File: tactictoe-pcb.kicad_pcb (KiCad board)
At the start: 4 copper layers, 85.6 x 54 mm, 90 parts, among them J1 USB_C_Receptacle_USB2.0_16P, J2 Conn_01x04, T1 Touchpad, T2 Touchpad, T3 Touchpad, T4 Touchpad, T5 Touchpad, T6 Touchpad, T7 Touchpad, T8 Touchpad, T9 Touchpad, U2 TLV74033PDBVR

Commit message: major v2 changes
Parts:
- removed R1, R2, R3: 10k, Resistor_SMD:R_0603_1608Metric_Pad0.98x0.95mm_HandSolder
- removed TP1: NRST, TestPoint:TestPoint_Pad_D1.0mm
- removed TP2: PF0, TestPoint:TestPoint_Pad_D1.0mm
- removed TP3: PF1, TestPoint:TestPoint_Pad_D1.0mm
- removed TP4: PB8, TestPoint:TestPoint_Pad_D1.0mm
- removed TP5: PA15, TestPoint:TestPoint_Pad_D1.0mm
- C1, C2, C3, C4, C5, C6, C7, C8, C9: footprint Capacitor_SMD:C_0603_1608Metric_Pad1.08x0.95mm_HandSolder -> Capacitor_SMD:C_0603_1608Metric
- D1, D10, D11, D12, D13, D14, D15, D16, D17, D18, D19, D2, D20, D21, D22, D23, D24, D25, D26, D27, D28, D29, D3, D30, D31, D32, D33, D34, D35, D36, D37, D38, D39, D4, D40, D41, D42, D43, D44, D45, D5, D6, D7, D8, D9: value SK6805-EC15 -> XL-1615RGBC; footprint tictactoe-bolt-footprints:SK6805-EC15 -> tactictoe-footprints:XL-1615RGBC-WS2812B-S
- J1: footprint tictactoe-bolt-footprints:USB_C_Receptacle_TYPE-C-16P-CB1-6-073 -> tactictoe-footprints:USB_C_Receptacle_TYPE-C-16P-CB1-6-073
- J2: footprint Connector_PinHeader_2.54mm:PinHeader_1x04_P2.54mm_Vertical -> tactictoe-footprints:tactictoe-sw-pins; moved to B.Cu
- R10, R11, R12, R13, R14, R4, R5, R6, R7, R8, R9: footprint Resistor_SMD:R_0603_1608Metric_Pad0.98x0.95mm_HandSolder -> Resistor_SMD:R_0603_1608Metric
- T1, T2, T3, T4, T5, T6, T7, T8, T9: footprint tictactoe-bolt-footprints:Touch-pad -> tactictoe-footprints:Touch-pad_XL-1615
- U1: value ~ -> F042G6U6TR
- moved R6 21.5 mm to (117.0, 103.1), turned to -90 degrees
- moved R7 19.4 mm to (118.5, 103.1), turned to -90 degrees
- moved R8 17.3 mm to (120.0, 103.1), turned to -90 degrees
- moved C6 15.1 mm to (115.2, 110.8)
- moved C7 15.1 mm to (113.7, 110.8)
- moved C5 14.0 mm to (123.0, 112.0)
- moved C9 14.0 mm to (124.5, 112.0)
- moved U1 14.0 mm to (119.0, 111.0)
- moved C3 13.4 mm to (117.0, 116.9)
- moved C4 13.4 mm to (115.5, 116.9)
- moved C1 11.5 mm to (108.3, 107.0), turned to -90 degrees
- moved R14 11.1 mm to (119.9, 116.9), turned to 90 degrees
- moved C8 10.8 mm to (123.0, 103.1), turned to 90 degrees
- moved R13 9.15 mm to (121.4, 116.9), turned to 90 degrees
- moved R12 7.28 mm to (122.9, 116.9), turned to 90 degrees
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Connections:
- D1 pad 1: /LED_CH4 -> GND
- D1 pad 2: +5V -> /LED_T3C4
- D1 pad 3: Net-(D1-DOUT) -> +5V
- D1 pad 4: GND -> Net-(D1-DOUT)
- D10 pad 1: Net-(D10-DIN) -> GND
- D10 pad 2: +5V -> Net-(D10-DIN)
- D10 pad 3: Net-(D10-DOUT) -> +5V
- D10 pad 4: GND -> Net-(D10-DOUT)
- D11 pad 1: Net-(D10-DOUT) -> GND
- D11 pad 2: +5V -> Net-(D10-DOUT)
- D11 pad 3: Net-(D11-DOUT) -> +5V
- D11 pad 4: GND -> Net-(D11-DOUT)
- D12 pad 1: Net-(D11-DOUT) -> GND
- D12 pad 2: +5V -> Net-(D11-DOUT)
- D12 pad 3: Net-(D12-DOUT) -> +5V
- D12 pad 4: GND -> Net-(D12-DOUT)
- D13 pad 1: Net-(D12-DOUT) -> GND
- D13 pad 2: +5V -> Net-(D12-DOUT)
- D13 pad 3: Net-(D13-DOUT) -> +5V
- D13 pad 4: GND -> Net-(D13-DOUT)
- D14 pad 1: Net-(D13-DOUT) -> GND
- D14 pad 2: +5V -> Net-(D13-DOUT)
- D14 pad 3: Net-(D14-DOUT) -> +5V
- D14 pad 4: GND -> Net-(D14-DOUT)
- D15 pad 1: Net-(D14-DOUT) -> GND
- D15 pad 2: +5V -> Net-(D14-DOUT)
- D15 pad 3: unconnected-(D15-DOUT-Pad3) -> +5V
- D15 pad 4: GND -> unconnected-(D15-DOUT-Pad4)
- D16 pad 1: /LED_CH3 -> GND
- D16 pad 2: +5V -> /LED_T3C3
- D16 pad 3: Net-(D16-DOUT) -> +5V
- D16 pad 4: GND -> Net-(D16-DOUT)
- D17 pad 1: Net-(D16-DOUT) -> GND
- D17 pad 2: +5V -> Net-(D16-DOUT)
- D17 pad 3: Net-(D17-DOUT) -> +5V
- D17 pad 4: GND -> Net-(D17-DOUT)
- D18 pad 1: Net-(D17-DOUT) -> GND
- D18 pad 2: +5V -> Net-(D17-DOUT)
- D18 pad 3: Net-(D18-DOUT) -> +5V
- D18 pad 4: GND -> Net-(D18-DOUT)
- D19 pad 1: Net-(D18-DOUT) -> GND
- D19 pad 2: +5V -> Net-(D18-DOUT)
- D19 pad 3: Net-(D19-DOUT) -> +5V
- D19 pad 4: GND -> Net-(D19-DOUT)
- D2 pad 1: Net-(D1-DOUT) -> GND
- D2 pad 2: +5V -> Net-(D1-DOUT)
- D2 pad 3: Net-(D2-DOUT) -> +5V
- D2 pad 4: GND -> Net-(D2-DOUT)
- D20 pad 1: Net-(D19-DOUT) -> GND
- D20 pad 2: +5V -> Net-(D19-DOUT)
- D20 pad 3: Net-(D20-DOUT) -> +5V
- D20 pad 4: GND -> Net-(D20-DOUT)
- D21 pad 1: Net-(D20-DOUT) -> GND
- D21 pad 2: +5V -> Net-(D20-DOUT)
- D21 pad 3: Net-(D21-DOUT) -> +5V
- D21 pad 4: GND -> Net-(D21-DOUT)
- D22 pad 1: Net-(D21-DOUT) -> GND
- D22 pad 2: +5V -> Net-(D21-DOUT)
- D22 pad 3: Net-(D22-DOUT) -> +5V
- D22 pad 4: GND -> Net-(D22-DOUT)
- D23 pad 1: Net-(D22-DOUT) -> GND
- D23 pad 2: +5V -> Net-(D22-DOUT)
- D23 pad 3: Net-(D23-DOUT) -> +5V
- D23 pad 4: GND -> Net-(D23-DOUT)
- D24 pad 1: Net-(D23-DOUT) -> GND
- D24 pad 2: +5V -> Net-(D23-DOUT)
- D24 pad 3: Net-(D24-DOUT) -> +5V
- D24 pad 4: GND -> Net-(D24-DOUT)
- D25 pad 1: Net-(D24-DOUT) -> GND
- D25 pad 2: +5V -> Net-(D24-DOUT)
- D25 pad 3: Net-(D25-DOUT) -> +5V
- D25 pad 4: GND -> Net-(D25-DOUT)
- D26 pad 1: Net-(D25-DOUT) -> GND
- D26 pad 2: +5V -> Net-(D25-DOUT)
- D26 pad 3: Net-(D26-DOUT) -> +5V
- D26 pad 4: GND -> Net-(D26-DOUT)
- D27 pad 1: Net-(D26-DOUT) -> GND
- D27 pad 2: +5V -> Net-(D26-DOUT)
- D27 pad 3: Net-(D27-DOUT) -> +5V
- D27 pad 4: GND -> Net-(D27-DOUT)
- D28 pad 1: Net-(D27-DOUT) -> GND
- D28 pad 2: +5V -> Net-(D27-DOUT)
- D28 pad 3: Net-(D28-DOUT) -> +5V
- D28 pad 4: GND -> Net-(D28-DOUT)
- D29 pad 1: Net-(D28-DOUT) -> GND
- D29 pad 2: +5V -> Net-(D28-DOUT)
- D29 pad 3: Net-(D29-DOUT) -> +5V
- D29 pad 4: GND -> Net-(D29-DOUT)
- D3 pad 1: Net-(D2-DOUT) -> GND
- D3 pad 2: +5V -> Net-(D2-DOUT)
- D3 pad 3: Net-(D3-DOUT) -> +5V
- D3 pad 4: GND -> Net-(D3-DOUT)
- D30 pad 1: Net-(D29-DOUT) -> GND
- D30 pad 2: +5V -> Net-(D29-DOUT)
- D30 pad 3: unconnected-(D30-DOUT-Pad3) -> +5V
- D30 pad 4: GND -> unconnected-(D30-DOUT-Pad4)
- D31 pad 1: /LED_CH2 -> GND
- D31 pad 2: +5V -> /LED_T16C1
- D31 pad 3: Net-(D31-DOUT) -> +5V
- D31 pad 4: GND -> Net-(D31-DOUT)
- D32 pad 1: Net-(D31-DOUT) -> GND
- D32 pad 2: +5V -> Net-(D31-DOUT)
- D32 pad 3: Net-(D32-DOUT) -> +5V
- D32 pad 4: GND -> Net-(D32-DOUT)
- D33 pad 1: Net-(D32-DOUT) -> GND
- D33 pad 2: +5V -> Net-(D32-DOUT)
- D33 pad 3: Net-(D33-DOUT) -> +5V
- D33 pad 4: GND -> Net-(D33-DOUT)
- D34 pad 1: Net-(D33-DOUT) -> GND
- D34 pad 2: +5V -> Net-(D33-DOUT)
- D34 pad 3: Net-(D34-DOUT) -> +5V
- D34 pad 4: GND -> Net-(D34-DOUT)
- D35 pad 1: Net-(D34-DOUT) -> GND
- D35 pad 2: +5V -> Net-(D34-DOUT)
- D35 pad 3: Net-(D35-DOUT) -> +5V
- D35 pad 4: GND -> Net-(D35-DOUT)
- D36 pad 1: Net-(D35-DOUT) -> GND
- D36 pad 2: +5V -> Net-(D35-DOUT)
- D36 pad 3: Net-(D36-DOUT) -> +5V
- D36 pad 4: GND -> Net-(D36-DOUT)
- D37 pad 1: Net-(D36-DOUT) -> GND
- D37 pad 2: +5V -> Net-(D36-DOUT)
- D37 pad 3: Net-(D37-DOUT) -> +5V
- D37 pad 4: GND -> Net-(D37-DOUT)
- D38 pad 1: Net-(D37-DOUT) -> GND
- D38 pad 2: +5V -> Net-(D37-DOUT)
- D38 pad 3: Net-(D38-DOUT) -> +5V
- D38 pad 4: GND -> Net-(D38-DOUT)
- D39 pad 1: Net-(D38-DOUT) -> GND
- D39 pad 2: +5V -> Net-(D38-DOUT)
- D39 pad 3: Net-(D39-DOUT) -> +5V
- D39 pad 4: GND -> Net-(D39-DOUT)
- D4 pad 1: Net-(D3-DOUT) -> GND
- D4 pad 2: +5V -> Net-(D3-DOUT)
- D4 pad 3: Net-(D4-DOUT) -> +5V
- D4 pad 4: GND -> Net-(D4-DOUT)
- D40 pad 1: Net-(D39-DOUT) -> GND
- D40 pad 2: +5V -> Net-(D39-DOUT)
- D40 pad 3: Net-(D40-DOUT) -> +5V
- D40 pad 4: GND -> Net-(D40-DOUT)
- D41 pad 1: Net-(D40-DOUT) -> GND
- D41 pad 2: +5V -> Net-(D40-DOUT)
- D41 pad 3: Net-(D41-DOUT) -> +5V
- D41 pad 4: GND -> Net-(D41-DOUT)
- D42 pad 1: Net-(D41-DOUT) -> GND
- D42 pad 2: +5V -> Net-(D41-DOUT)
- D42 pad 3: Net-(D42-DOUT) -> +5V
- D42 pad 4: GND -> Net-(D42-DOUT)
- D43 pad 1: Net-(D42-DOUT) -> GND
- D43 pad 2: +5V -> Net-(D42-DOUT)
- D43 pad 3: Net-(D43-DOUT) -> +5V
- D43 pad 4: GND -> Net-(D43-DOUT)
- D44 pad 1: Net-(D43-DOUT) -> GND
- D44 pad 2: +5V -> Net-(D43-DOUT)
- D44 pad 3: Net-(D44-DOUT) -> +5V
- D44 pad 4: GND -> Net-(D44-DOUT)
- D45 pad 1: Net-(D44-DOUT) -> GND
- D45 pad 2: +5V -> Net-(D44-DOUT)
- D45 pad 3: unconnected-(D45-DOUT-Pad3) -> +5V
- D45 pad 4: GND -> unconnected-(D45-DOUT-Pad4)
- D5 pad 1: Net-(D4-DOUT) -> GND
- D5 pad 2: +5V -> Net-(D4-DOUT)
- D5 pad 3: Net-(D5-DOUT) -> +5V
- D5 pad 4: GND -> Net-(D5-DOUT)
- D6 pad 1: Net-(D5-DOUT) -> GND
- D6 pad 2: +5V -> Net-(D5-DOUT)
- D6 pad 3: Net-(D6-DOUT) -> +5V
- D6 pad 4: GND -> Net-(D6-DOUT)
- D7 pad 1: Net-(D6-DOUT) -> GND
- D7 pad 2: +5V -> Net-(D6-DOUT)
- D7 pad 3: Net-(D7-DOUT) -> +5V
- D7 pad 4: GND -> Net-(D7-DOUT)
- D8 pad 1: Net-(D7-DOUT) -> GND
- D8 pad 2: +5V -> Net-(D7-DOUT)
- D8 pad 3: Net-(D8-DOUT) -> +5V
- D8 pad 4: GND -> Net-(D8-DOUT)
- D9 pad 1: Net-(D8-DOUT) -> GND
- D9 pad 2: +5V -> Net-(D8-DOUT)
- D9 pad 3: Net-(D10-DIN) -> +5V
- D9 pad 4: GND -> Net-(D10-DIN)
- J1 pad A6: /USB_D+ -> unconnected-(J1-D+-PadA6)
- J1 pad A7: /USB_D- -> unconnected-(J1-D--PadA7)
- J1 pad B6: /USB_D+ -> unconnected-(J1-D+-PadB6)
- J1 pad B7: /USB_D- -> unconnected-(J1-D--PadB7)
- J2 pad 1: +5V -> GND
- J2 pad 4: GND -> +5V
- U1 pad 1: /PB8 -> /LED_T16C1
- U1 pad 14: /LED_CH3 -> /LED_T3C3
- U1 pad 15: /LED_CH4 -> /LED_T3C4
- U1 pad 19: /USB_D- -> unconnected-(U1-PA9/PA11-Pad19)
- U1 pad 2: /PF0 -> unconnected-(U1-PF0-Pad2)
- U1 pad 20: /USB_D+ -> unconnected-(U1-PA10/PA12-Pad20)
- U1 pad 23: /PA15 -> unconnected-(U1-PA15-Pad23)
- U1 pad 26: /LED_CH2 -> unconnected-(U1-PB5-Pad26)
- U1 pad 3: /PF1 -> unconnected-(U1-PF1-Pad3)
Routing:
- net /LED_CH4: track 34.9 -> 0.00 mm
- net /TSC_G3_IO2: track 31.0 -> 0.00 mm
- net /BTN_9: track 44.5 -> 14.9 mm
- net /LED_CH2: track 28.6 -> 0.00 mm, vias 2 -> 0
- net /TSC_G3_IO3: track 28.3 -> 0.00 mm
- net /TSC_G3_IO4: track 26.1 -> 0.00 mm
- net /LED_CH3: track 23.7 -> 0.00 mm, vias 2 -> 0
- net /SWCLK: track 20.6 -> 0.00 mm
- net /SWDIO: track 18.0 -> 0.00 mm
- net /TSC_G2_IO4: track 17.6 -> 0.00 mm
- net /TSC_G1_IO4: track 16.2 -> 0.00 mm
- net /TSC_G2_IO3: track 15.8 -> 0.00 mm
- net /TSC_G1_IO3: track 15.5 -> 0.00 mm
- net /TSC_G1_IO2: track 15.4 -> 0.00 mm
- net /TSC_G2_IO2: track 13.8 -> 0.00 mm
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- added copper zone on In2.Cu, net +3V3
- added copper zone on In2.Cu, net +5V
- added copper zone on B.Cu, net GND
- added copper zone on In1.Cu, net GND
- removed copper zone on B.Cu, net +3V3
- removed copper zone on B.Cu, net +5V
- removed copper zone on In2.Cu, net GND
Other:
- board text added: "Sensor Demo"
- board text added: "VS AI"
- board text added: "VS Player"

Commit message: v2 fully routed
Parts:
- J2: moved to F.Cu
- turned J2 to 180 degrees
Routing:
- net /LED_T3C4: track 0.00 -> 46.4 mm, vias 1 -> 2
- net /BTN_9: track 14.9 -> 56.4 mm
- net /BTN_1: track 2.57 -> 37.8 mm
- net /LED_T3C3: track 1.45 -> 34.0 mm
- net /BTN_2: track 27.3 -> 46.2 mm
- net /LED_T16C1: track 0.00 -> 17.6 mm, vias 1 -> 2
- net /BTN_3: track 43.5 -> 59.6 mm
- net /BTN_7: track 2.57 -> 17.6 mm
- net /BTN_8: track 23.0 -> 37.2 mm
- net /SWCLK: track 0.00 -> 12.5 mm
- net /SWDIO: track 0.00 -> 11.2 mm
- net /NRST: track 2.16 -> 10.0 mm
- net /TSC_G2_CS: track 0.00 -> 7.15 mm
- net /BTN_6: track 43.5 -> 50.5 mm
- net /BTN_4: track 10.3 -> 17.1 mm
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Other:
- board text added: "5V"
- board text added: "CK"
- board text added: "GND"
- board text added: "IO"
- board text added: "Player VS AI"
- board text added: "Player VS Player"
- board text added: "Swap Player"
- board text added: "tic-tac-toe with 3-mark limit"
- board text removed: "Long press middle button to change modes: 1) vs Easy AI 2) vs Impossible AI 2) vs Player"
- board text removed: "Sensor Demo"
- board text removed: "TACTIC-TOE"
- board text removed: "V1"
- board text removed: "VS AI"
- board text removed: "VS Player"

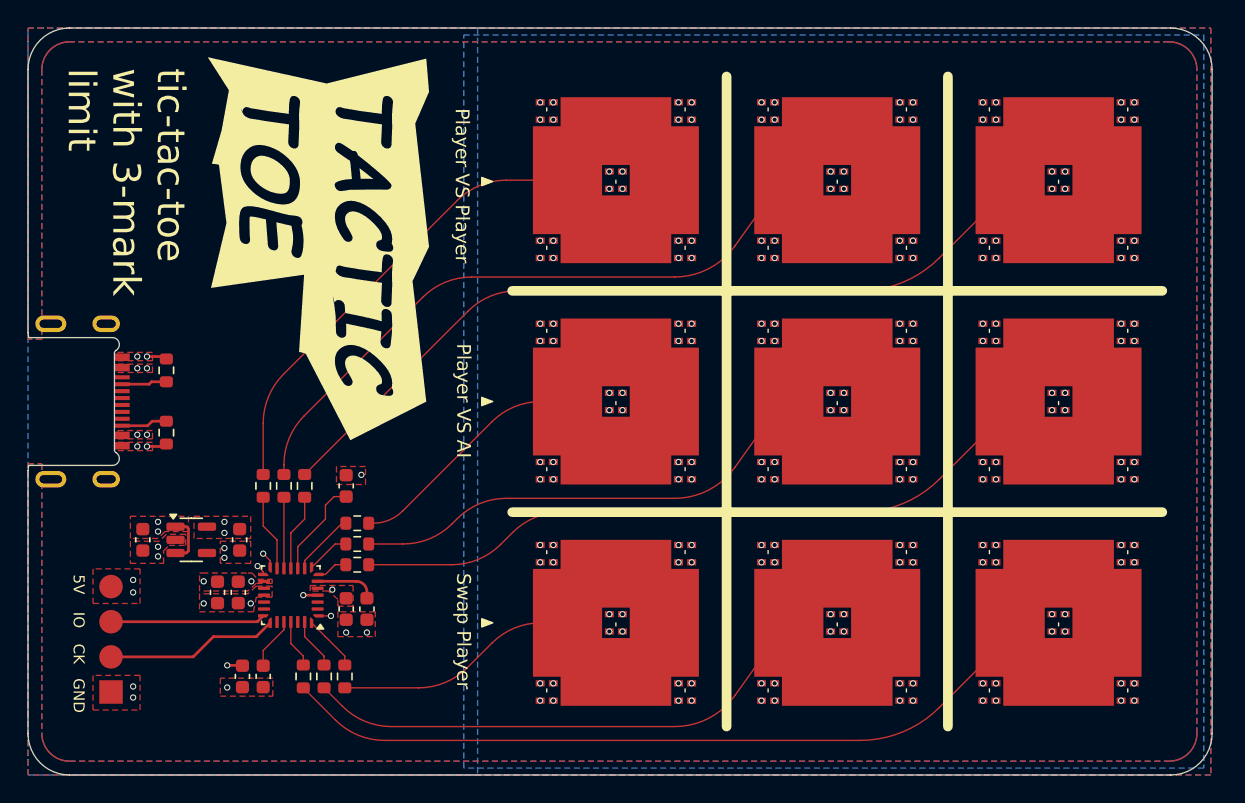
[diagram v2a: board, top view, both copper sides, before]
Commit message: silkscreen cleanup, v2 first gerber candidate
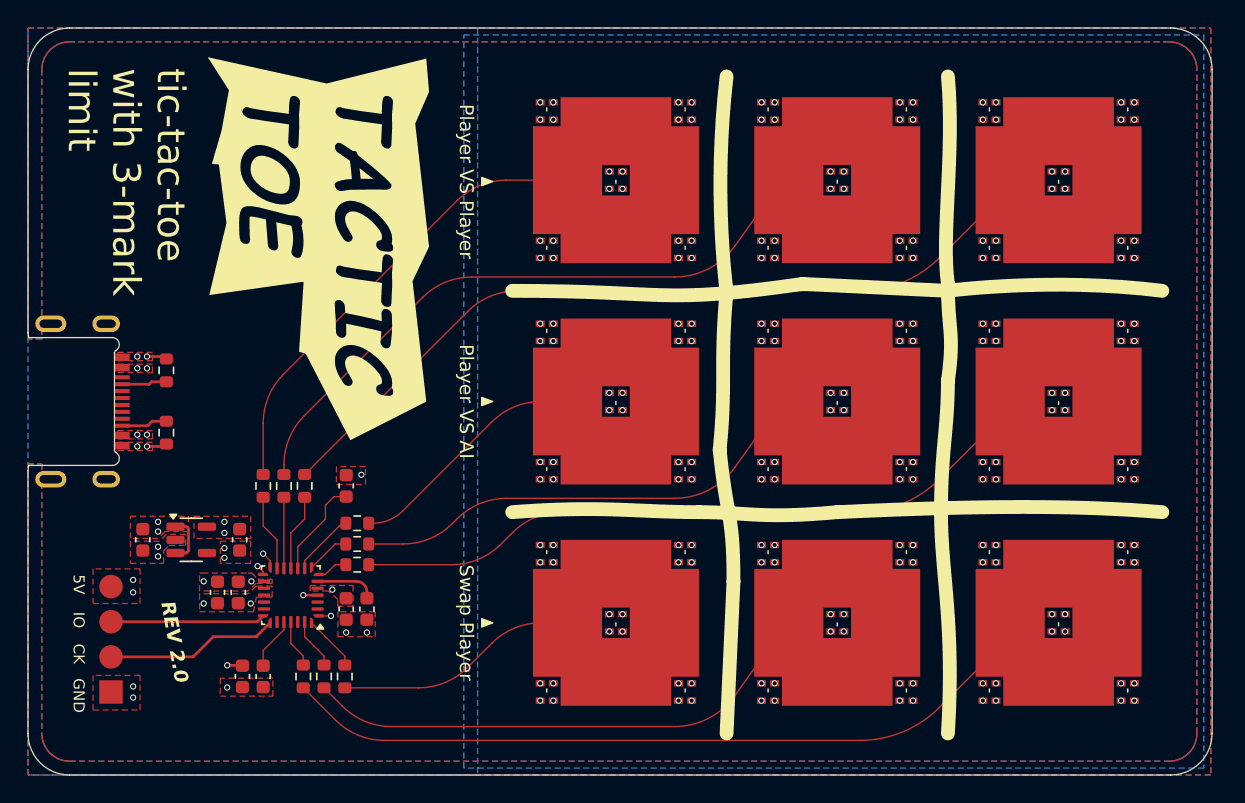
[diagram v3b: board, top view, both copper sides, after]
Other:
- board text added: "REV 2.0"

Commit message: fixed linkedin id typo
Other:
- board text added: "Amrlxyz in/amierulhakeem amierulhakeem02@gmail.com"
- board text removed: "Amrlxyz in/amierulhakeem02 amierulhakeem02@gmail.com"
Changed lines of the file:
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@@
 		)
 	)
-	(gr_text "Amrlxyz\nin/amierulhakeem02\namierulhakeem02@gmail.com"
+	(gr_text "Amrlxyz\nin/amierulhakeem\namierulhakeem02@gmail.com"
 		(at 112 118.5 0)
 		(layer "B.SilkS")
